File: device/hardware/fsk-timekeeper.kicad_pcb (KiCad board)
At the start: 2 copper layers, 92 x 57 mm, 27 parts, among them J1 SENSOR, SW1 SW_SPST, U1 SuperMini nRF52840, U2 Ai-Thinker Ra-01SH, U3 TPS61040DBV, U4 ATGM336H

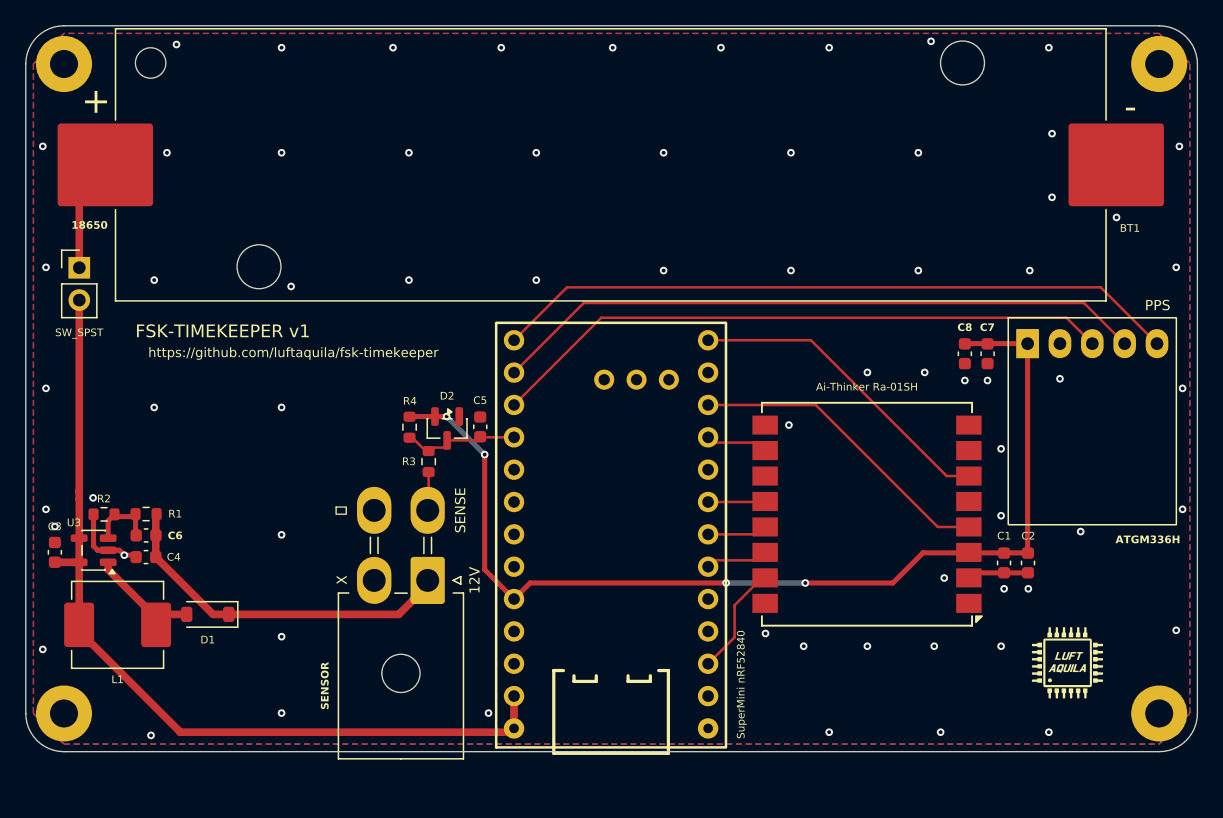
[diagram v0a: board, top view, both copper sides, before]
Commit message: fix(hardware): update PCB layout and fit master and sensor housings
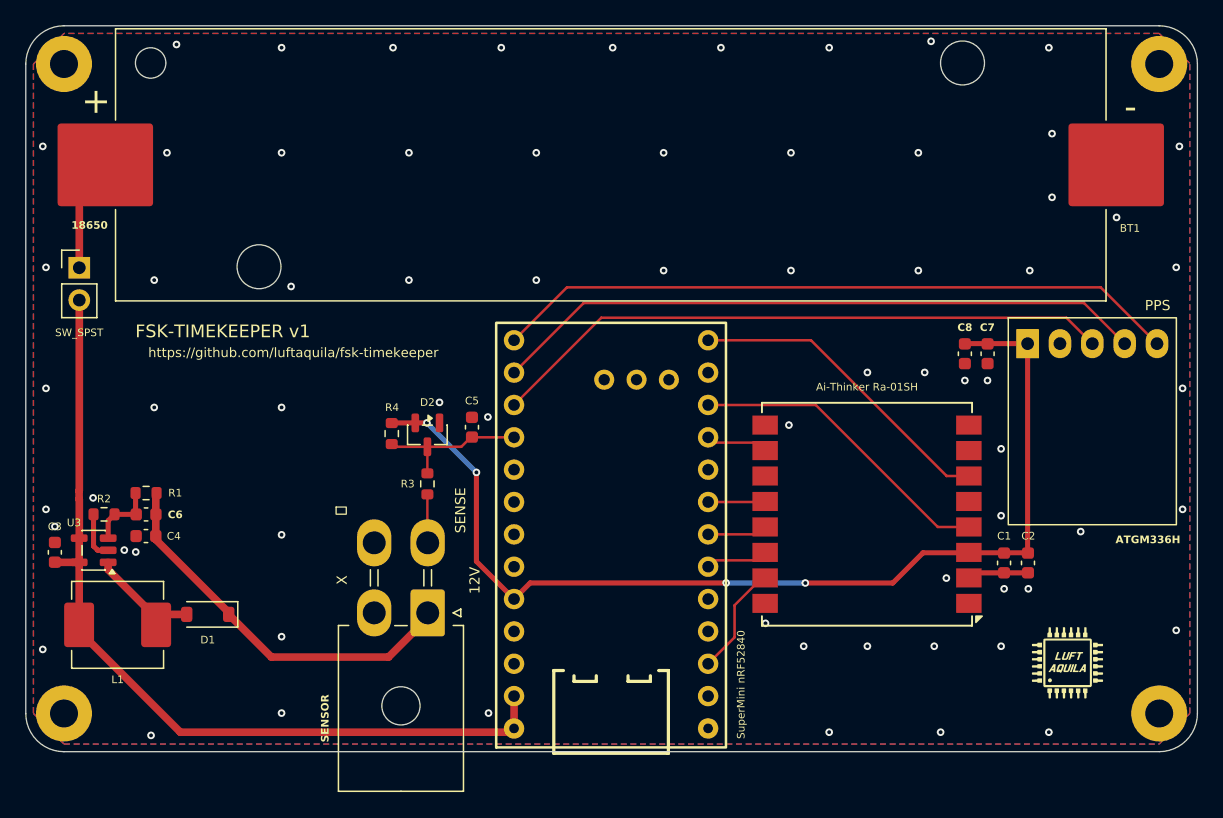
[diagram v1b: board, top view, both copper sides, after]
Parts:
- moved J1 2.55 mm to (132.7, 115.6)
- moved R3 1.75 mm to (132.7, 105.5)
- moved C4 1.65 mm to (110.6, 109.6)
- moved R1 1.65 mm to (110.6, 106.2)
- moved C6 1.65 mm to (110.6, 107.9)
- moved D2 1.63 mm to (132.7, 101.7)
- moved R4 1.49 mm to (129.9, 101.5)
- moved C5 0.65 mm to (136.2, 101.0)
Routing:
- net /SENSOR: track 7.80 -> 11.9 mm
- net +12V: track 27.5 -> 30.5 mm
- net GND: track 10.2 -> 7.99 mm, vias 67 -> 69
- net /SENSE: track 2.93 -> 3.81 mm
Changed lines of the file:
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@@
 	(footprint "Connector_Molex:Molex_Mini-Fit_Jr_5569-04A2_2x02_P4.20mm_Horizontal"
 		(layer "F.Cu")
-		(at 132.724 113.0808 180)
+		(at 132.724 115.63 180)
 		(descr "Molex Mini-Fit Jr. Power Connectors, old mpn/engineering number: 5569-04A2, example for new mpn: 39-30-0040, 2 Pins per row, Mounting: Snap-in Plastic Peg PCB Lock (http://www.molex.com/pdm_docs/sd/039300020_sd.pdf)")
 		(tags "connector Molex Mini-Fit_Jr horizontalplastic_peg")
@@
 	(footprint "Package_TO_SOT_SMD:SOT-23"
 		(layer "F.Cu")
-		(at 134.25 101.15 -90)
+		(at 132.7 101.65 -90)
 		(descr "SOT, 3 Pin (JEDEC TO-236 Var AB https://www.jedec.org/document_search?search_api_views_fulltext=TO-236)")
 		(tags "SOT TO_SOT_SMD")
@@
 	(footprint "Capacitor_SMD:C_0603_1608Metric"
 		(layer "F.Cu")
-		(at 110.6 111.25 180)
+		(at 110.6 109.6 180)
 		(descr "Capacitor SMD 0603 (1608 Metric), square (rectangular) end terminal, IPC-7351 nominal, (Body size source: IPC-SM-782 page 76, https://www.pcb-3d.com/wordpress/wp-content/uploads/ipc-sm-782a_amendment_1_and_2.pdf)")
 		(tags "capacitor")
@@
 	(footprint "Resistor_SMD:R_0603_1608Metric"
 		(layer "F.Cu")
-		(at 131.3 101.05 90)
+		(at 129.9 101.55 90)
 		(descr "Resistor SMD 0603 (1608 Metric), square (rectangular) end terminal, IPC-7351 nominal, (Body size source: IPC-SM-782 page 72, https://www.pcb-3d.com/wordpress/wp-content/uploads/ipc-sm-782a_amendment_1_and_2.pdf)")
 		(tags "resistor")
@@
 	(footprint "Resistor_SMD:R_0603_1608Metric"
 		(layer "F.Cu")
-		(at 110.6102 107.8709 180)
+		(at 110.6102 106.2209 180)
 		(descr "Resistor SMD 0603 (1608 Metric), square (rectangular) end terminal, IPC-7351 nominal, (Body size source: IPC-SM-782 page 72, https://www.pcb-3d.com/wordpress/wp-content/uploads/ipc-sm-782a_amendment_1_and_2.pdf)")
 		(tags "resistor")
@@
 	(footprint "Capacitor_SMD:C_0603_1608Metric"
 		(layer "F.Cu")
-		(at 110.6102 109.55 180)
+		(at 110.6102 107.9 180)
 		(descr "Capacitor SMD 0603 (1608 Metric), square (rectangular) end terminal, IPC-7351 nominal, (Body size source: IPC-SM-782 page 76, https://www.pcb-3d.com/wordpress/wp-content/uploads/ipc-sm-782a_amendment_1_and_2.pdf)")
 		(tags "capacitor")
@@
 	(footprint "Capacitor_SMD:C_0603_1608Metric"
 		(layer "F.Cu")
-		(at 136.85 101.025 90)
+		(at 136.2 101.05 90)
 		(descr "Capacitor SMD 0603 (1608 Metric), square (rectangular) end terminal, IPC-7351 nominal, (Body size source: IPC-SM-782 page 76, https://www.pcb-3d.com/wordpress/wp-content/uploads/ipc-sm-782a_amendment_1_and_2.pdf)")
 		(tags "capacitor")
@@
 	(footprint "Resistor_SMD:R_0603_1608Metric"
 		(layer "F.Cu")
-		(at 132.8 103.75 90)
+		(at 132.7 105.5 90)
 		(descr "Resistor SMD 0603 (1608 Metric), square (rectangular) end terminal, IPC-7351 nominal, (Body size source: IPC-SM-782 page 72, https://www.pcb-3d.com/wordpress/wp-content/uploads/ipc-sm-782a_amendment_1_and_2.pdf)")
 		(tags "resistor")
@@
 	)
 	(segment
-		(start 134.2125 100.2125)
-		(end 133.3 100.2125)
+		(start 136.55 104.6)
+		(end 136.55 111.590958)
 		(width 0.4)
 		(layer "F.Cu")
@@
 	)
 	(segment
-		(start 133.3 100.2125)
-		(end 131.4125 100.2125)
+		(start 132.6625 100.7125)
+		(end 131.75 100.7125)
 		(width 0.4)
 		(layer "F.Cu")
@@
 	)
 	(segment
-		(start 137.2 103.2)
-		(end 137.2 112.240958)
+		(start 162.378525 113.284)
+		(end 169.243875 113.284)
 		(width 0.4)
 		(layer "F.Cu")
@@
 	)
 	(segment
-		(start 162.378525 113.284)
-		(end 169.243875 113.284)
+		(start 131.75 100.7125)
+		(end 129.9125 100.7125)
+		(width 0.4)
+		(layer "F.Cu")
+		(net "+3.3V")
+	)
+	(segment
+		(start 129.9125 100.7125)
+		(end 129.9 100.725)
 		(width 0.4)
 		(layer "F.Cu")
@@
 	)
 	(segment
-		(start 137.2 112.240958)
+		(start 136.55 111.590958)
 		(end 139.504 114.544958)
 		(width 0.4)
@@
 	)
 	(via
-		(at 134.2125 100.2125)
+		(at 132.6625 100.7125)
 		(size 0.6)
 		(drill 0.3)
@@
 	)
 	(via
-		(at 137.2 103.2)
+		(at 136.55 104.6)
 		(size 0.6)
 		(drill 0.3)
@@
 	)
 	(segment
-		(start 137.2 103.2)
-		(end 134.2125 100.2125)
+		(start 162.375325 113.2808)
+		(end 162.378525 113.284)
 		(width 0.4)
 		(layer "B.Cu")
@@
 	)
 	(segment
-		(start 162.375325 113.2808)
-		(end 162.378525 113.284)
+		(start 136.55 104.6)
+		(end 132.6625 100.7125)
 		(width 0.4)
 		(layer "B.Cu")
@@
 	)
 	(segment
-		(start 108.5125 110.7125)
-		(end 107.6329 110.7125)
-		(width 0.4)
-		(layer "F.Cu")
-		(net "GND")
-	)
-	(segment
 		(start 179.861275 112.484)
 		(end 175.648477 112.484)
@@
 	)
 	(segment
-		(start 108.9 111.1)
-		(end 109.675 111.1)
-		(width 0.4)
-		(layer "F.Cu")
-		(net "GND")
-	)
-	(segment
-		(start 108.9 111.1)
-		(end 108.5125 110.7125)
-		(width 0.4)
-		(layer "F.Cu")
-		(net "GND")
-	)
-	(segment
 		(start 106.8125 110.7125)
 		(end 106.4832 110.3832)
@@
 	)
 	(via
-		(at 173.286976 112.891501)
+		(at 173.45 112.9)
 		(size 0.6)
 		(drill 0.3)
@@
 	)
 	(via
-		(at 159.25 117.25)
+		(at 131.25 79.5)
 		(size 0.6)
 		(drill 0.3)
@@
 	)
 	(via
-		(at 131.25 79.5)
+		(at 133.65 99.1)
 		(size 0.6)
 		(drill 0.3)
 		(layers "F.Cu" "B.Cu")
+		(free yes)
 		(net "GND")
 	)
@@
 	)
 	(via
+		(at 137.45 100.25)
+		(size 0.6)
+		(drill 0.3)
+		(layers "F.Cu" "B.Cu")
+		(free yes)
+		(net "GND")
+	)
+	(via
 		(at 171.25 88.75)
 		(size 0.6)
@@
 	)
 	(via
-		(at 164.25 125)
+		(at 159.25 116.45)
 		(size 0.6)
 		(drill 0.3)
 		(layers "F.Cu" "B.Cu")
+		(free yes)
 		(net "GND")
 	)
 	(via
-		(at 103.45 108.85)
+		(at 164.25 125)
 		(size 0.6)
 		(drill 0.3)
@@
 	)
 	(via
-		(at 182.372 97.25)
+		(at 103.45 108.85)
 		(size 0.6)
 		(drill 0.3)
@@
 	)
 	(via
-		(at 108.9 111.1)
+		(at 109.8 110.85)
+		(size 0.6)
+		(drill 0.3)
+		(layers "F.Cu" "B.Cu")
+		(free yes)
+		(net "GND")
+	)
+	(via
+		(at 108.9 110.7)
 		(size 0.6)
 		(drill 0.3)
@@
 	)
 	(segment
-		(start 130.4548 115.75)
-		(end 115.875 115.75)
+		(start 117.1 115.75)
+		(end 120.45 119.1)
+		(width 0.6)
+		(layer "F.Cu")
+		(net "+12V")
+	)
+	(segment
+		(start 117.1 115.6)
+		(end 111.375 109.875)
+		(width 0.6)
+		(layer "F.Cu")
+		(net "+12V")
+	)
+	(segment
+		(start 111.375 109.6)
+		(end 111.375 106.2811)
 		(width 0.6)
 		(layer "F.Cu")
@@
 	)
 	(segment
-		(start 111.375 111.25)
-		(end 111.375 107.9311)
+		(start 120.45 119.1)
+		(end 129.65 119.1)
 		(width 0.6)
 		(layer "F.Cu")
@@
 	)
 	(segment
-		(start 132.724 113.4808)
-		(end 130.4548 115.75)
+		(start 132.724 116.026)
+		(end 132.724 115.63)
 		(width 0.6)
 		(layer "F.Cu")
@@
 	)
 	(segment
-		(start 115.875 115.75)
-		(end 111.375 111.25)
+		(start 111.375 109.875)
+		(end 111.375 109.6)
 		(width 0.6)
 		(layer "F.Cu")
@@
 	)
 	(segment
-		(start 132.8 104.575)
-		(end 132.8 107.5048)
+		(start 129.65 119.1)
+		(end 132.724 116.026)
+		(width 0.6)
+		(layer "F.Cu")
+		(net "+12V")
+	)
+	(segment
+		(start 117.1 115.75)
+		(end 117.1 115.6)
+		(width 0.6)
+		(layer "F.Cu")
+		(net "+12V")
+	)
+	(segment
+		(start 132.7 110.106)
+		(end 132.724 110.13)
 		(width 0.2)
 		(layer "F.Cu")
@@
 	)
 	(segment
-		(start 134.25 102.65)
-		(end 133.075 102.65)
+		(start 132.7 106.325)
+		(end 132.7 110.106)
 		(width 0.2)
 		(layer "F.Cu")
-		(net "/SENSOR")
+		(net "/SENSE")
 	)
 	(segment
-		(start 132.575 102.925)
-		(end 131.625 101.975)
+		(start 130.3375 102.5875)
+		(end 130.225 102.475)
 		(width 0.2)
 		(layer "F.Cu")
@@
 	)
 	(segment
-		(start 136.85 101.725)
-		(end 136.4875 102.0875)
+		(start 135.3625 102.5875)
+		(end 132.75 102.5875)
 		(width 0.2)
 		(layer "F.Cu")
@@
 	(segment
 		(start 139.504 101.844958)
-		(end 136.969958 101.844958)
+		(end 136.219958 101.844958)
 		(width 0.2)
 		(layer "F.Cu")
@@
 	)
 	(segment
-		(start 136.4875 102.0875)
-		(end 134.25 102.0875)
+		(start 132.7 102.5875)
+		(end 132.7 104.675)
+		(width 0.2)
+		(layer "F.Cu")
+		(net "/SENSOR")
+	)
+	(segment
+		(start 132.7 102.5875)
+		(end 130.1125 102.5875)
+		(width 0.2)
+		(layer "F.Cu")
+		(net "/SENSOR")
+	)
+	(segment
+		(start 136.219958 101.844958)
+		(end 136.2 101.825)
+		(width 0.2)
+		(layer "F.Cu")
+		(net "/SENSOR")
+	)
+	(segment
+		(start 136.2 101.75)
+		(end 135.3625 102.5875)
 		(width 0.2)
 		(layer "F.Cu")
@@
 	)
 	(segment
-		(start 108.3223 108.0709)
-		(end 109.5961 108.0709)
+		(start 107.6329 108.3932)
+		(end 108.1332 107.8929)
 		(width 0.4)
 		(layer "F.Cu")
@@
 	)
 	(segment
-		(start 107.6329 108.3932)
-		(end 108.1332 107.8929)
+		(start 108.1332 107.8929)
+		(end 109.8281 107.8929)
+		(width 0.4)
+		(layer "F.Cu")
+		(net "Net-(U3-FB)")
+	)
+	(segment
+		(start 109.8281 107.8929)
+		(end 109.8352 107.9)
 		(width 0.4)
 		(layer "F.Cu")
@@
 	)
 	(segment
-		(start 109.7852 107.8709)
-		(end 109.7852 109.5)
+		(start 109.7852 106.2209)
+		(end 109.7852 107.85)
 		(width 0.4)
 		(layer "F.Cu")

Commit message: fix(hardware): refine power routing and refresh fabrication files
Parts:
- SW1: value SW_SPST -> POWER
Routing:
- net GND: vias 69 -> 71
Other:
- board text added: "x"
- board text removed: "X"
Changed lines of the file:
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@@
 			)
 		)
-		(property "Value" "SW_SPST"
+		(property "Value" "POWER"
 			(at -0.0056 5.0944 0)
 			(layer "F.SilkS")
@@
 		(tags "SOT TO_SOT_SMD")
 		(property "Reference" "U3"
-			(at 1.5454 2.1625 0)
+			(at -2.8262 -0.9967 0)
 			(layer "F.SilkS")
 			(effects
@@
 		(tags "resistor")
 		(property "Reference" "R2"
-			(at 0.0038 1.2192 0)
+			(at 2.2538 -0.0063 0)
 			(layer "F.SilkS")
 			(effects
@@
 		)
 	)
-	(gr_text "X"
-		(at 126 113.05 90)
+	(gr_text "x"
+		(at 125.8316 115.5336 90)
 		(layer "F.SilkS")
 		(effects
@@
 	)
 	(gr_text "SENSE"
-		(at 135.3 107.5808 90)
+		(at 135.3 110.0644 90)
 		(layer "F.SilkS")
 		(effects
@@
 	)
 	(gr_text "12V"
-		(at 136.424 113.0808 90)
+		(at 136.424 115.5644 90)
 		(layer "F.SilkS")
 		(effects
@@
 	)
 	(gr_text "⏚"
-		(at 125.9 107.6 270)
+		(at 125.9 110.0836 270)
 		(layer "F.SilkS")
 		(effects
@@
 	)
 	(segment
+		(start 105.35 117.05)
+		(end 113.3696 125.0696)
+		(width 0.6)
+		(layer "F.Cu")
+		(net "+BATT")
+	)
+	(segment
 		(start 105.35 106.702271)
 		(end 105.35 106.039529)
@@
 	)
 	(segment
+		(start 113.3696 125.0696)
+		(end 139.139358 125.0696)
+		(width 0.6)
+		(layer "F.Cu")
+		(net "+BATT")
+	)
+	(segment
+		(start 139.139358 125.0696)
+		(end 139.208958 125)
+		(width 0.6)
+		(layer "F.Cu")
+		(net "+BATT")
+	)
+	(segment
 		(start 105.3579 111.6625)
 		(end 105.3579 109.7625)
@@
 	)
 	(segment
-		(start 113.3 125)
-		(end 139.208958 125)
-		(width 0.6)
-		(layer "F.Cu")
-		(net "+BATT")
-	)
-	(segment
 		(start 105.35 106.039529)
 		(end 105.3648 106.024729)
@@
 	)
 	(segment
-		(start 105.35 117.05)
-		(end 113.3 125)
-		(width 0.6)
-		(layer "F.Cu")
-		(net "+BATT")
-	)
-	(segment
 		(start 113.8 115.75)
 		(end 111.4 115.75)
@@
 	)
 	(via
+		(at 114.1984 123.4948)
+		(size 0.6)
+		(drill 0.3)
+		(layers "F.Cu" "B.Cu")
+		(net "GND")
+	)
+	(via
 		(at 106.45 106.6)
 		(size 0.6)
@@
 		(net "GND")
 	)
+	(via
+		(at 113.792 109.5756)
+		(size 0.6)
+		(drill 0.3)
+		(layers "F.Cu" "B.Cu")
+		(net "GND")
+	)
 	(segment
 		(start 182.879 92.456)
@@
 	)
 	(segment
-		(start 117.1 115.75)
-		(end 120.45 119.1)
+		(start 117.1 115.6)
+		(end 111.375 109.875)
 		(width 0.6)
 		(layer "F.Cu")
@@
 	)
 	(segment
-		(start 117.1 115.6)
-		(end 111.375 109.875)
+		(start 132.724 116.026)
+		(end 132.724 115.63)
 		(width 0.6)
 		(layer "F.Cu")
@@
 	)
 	(segment
-		(start 120.45 119.1)
-		(end 129.65 119.1)
+		(start 111.375 109.875)
+		(end 111.375 109.6)
 		(width 0.6)
 		(layer "F.Cu")
@@
 	)
 	(segment
-		(start 132.724 116.026)
-		(end 132.724 115.63)
+		(start 120.3236 118.9736)
+		(end 129.7764 118.9736)
 		(width 0.6)
 		(layer "F.Cu")
@@
 	)
 	(segment
-		(start 111.375 109.875)
-		(end 111.375 109.6)
+		(start 129.7764 118.9736)
+		(end 132.724 116.026)
 		(width 0.6)
 		(layer "F.Cu")
@@
 	)
 	(segment
-		(start 129.65 119.1)
-		(end 132.724 116.026)
+		(start 117.1 115.75)
+		(end 120.3236 118.9736)
 		(width 0.6)
 		(layer "F.Cu")
@@
 	)
 	(zone
+		(layer "F.Cu")
+		(hatch edge 0.5)
+		(connect_pads
+			(clearance 0)
+		)
+		(min_thickness 0.25)
+		(keepout
+			(tracks allowed)
+			(vias allowed)
+			(pads allowed)
+			(copperpour not_allowed)
+			(footprints allowed)
+		)
+		(placement
+			(enabled no)
+			(sheetname "")
+		)
+		(fill
+			(thermal_gap 0.5)
+			(thermal_bridge_width 0.5)
+			(island_removal_mode 0)
+		)
+		(polygon
+			(pts
+				(xy 104.5972 112.9792) (xy 104.5972 120.142) (xy 112.1664 120.142) (xy 112.1664 114.7064)
+			)
+		)
+	)
+	(zone
